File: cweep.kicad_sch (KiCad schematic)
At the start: 51 parts

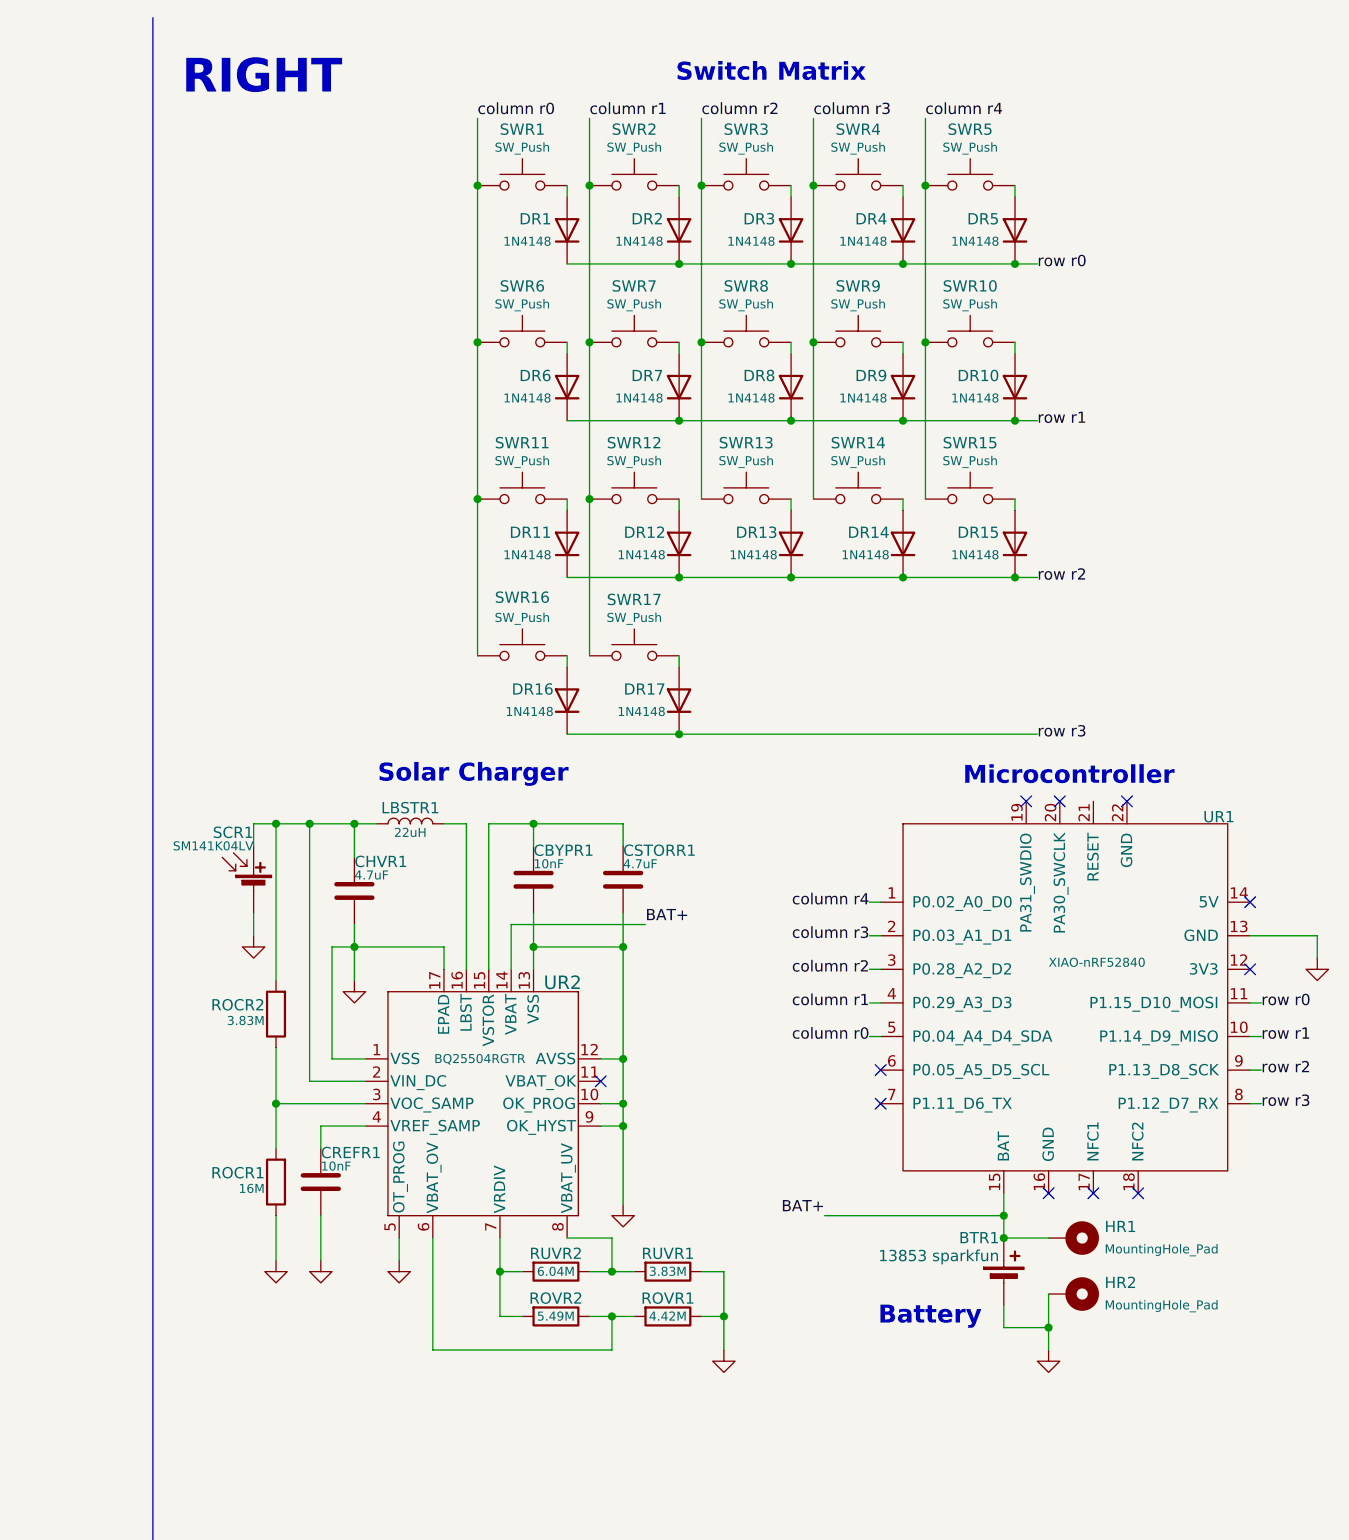
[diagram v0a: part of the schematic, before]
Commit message: feat: add reset button and power switch
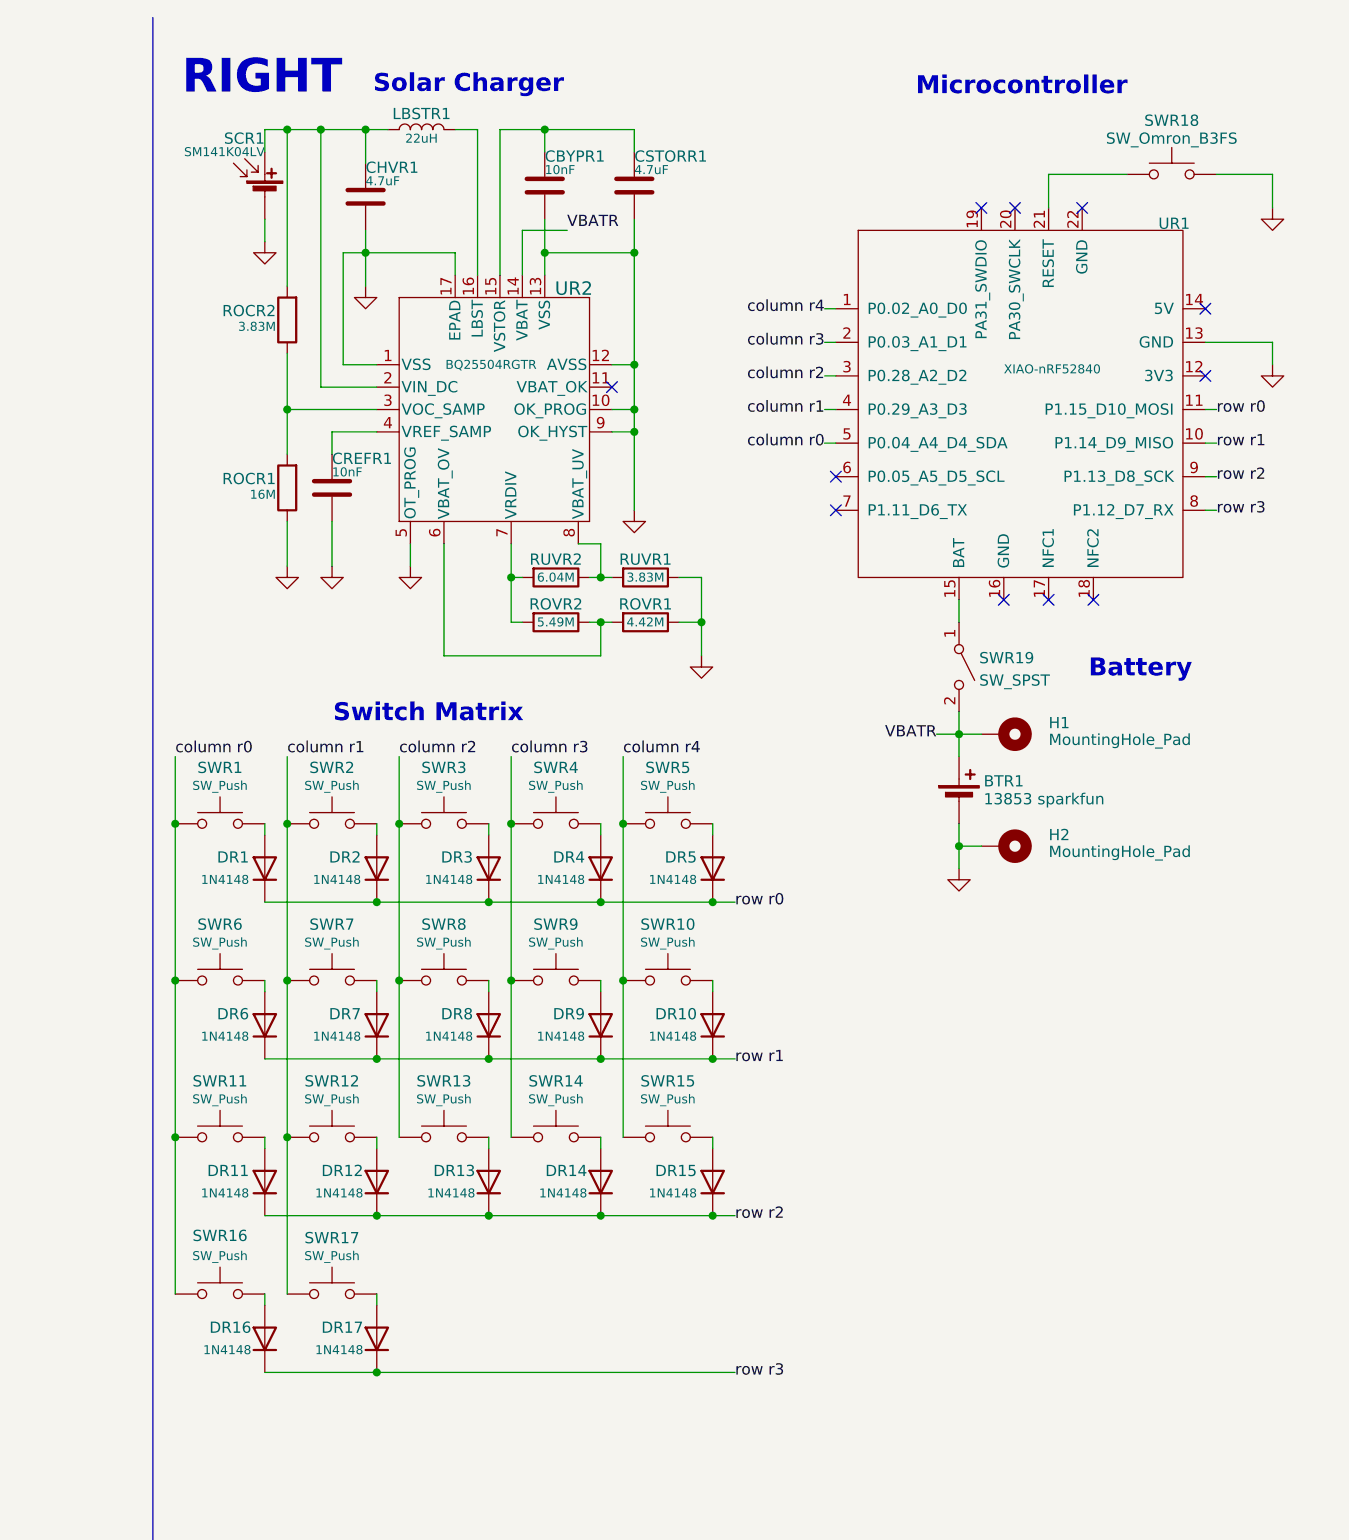
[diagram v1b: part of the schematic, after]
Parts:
- added SWR18: SW_Omron_B3FS, Button_Switch_THT:SW_TH_Tactile_Omron_B3F-10xx, symbol Switch:SW_Omron_B3FS
- added SWR19: SW_SPST, KAN-15:SW_KAN-15_PHT, symbol Switch:SW_SPST
- renumbered HR1 to H1, HR2 to H2
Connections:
- net GND: now also SWR18.2
- net at UR1.21 (RESET): now also SWR18.1
- net BAT+ renamed VBATR
- net VBATR: now also SWR19.2 (B); no longer UR1.15 (BAT)
- new net: SWR19.1 (A), UR1.15 (BAT)
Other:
- moved on the sheet: BTR1, CBYPR1, CHVR1, CREFR1, CSTORR1, DR1, DR10, DR11, DR12, DR13, DR14, DR15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

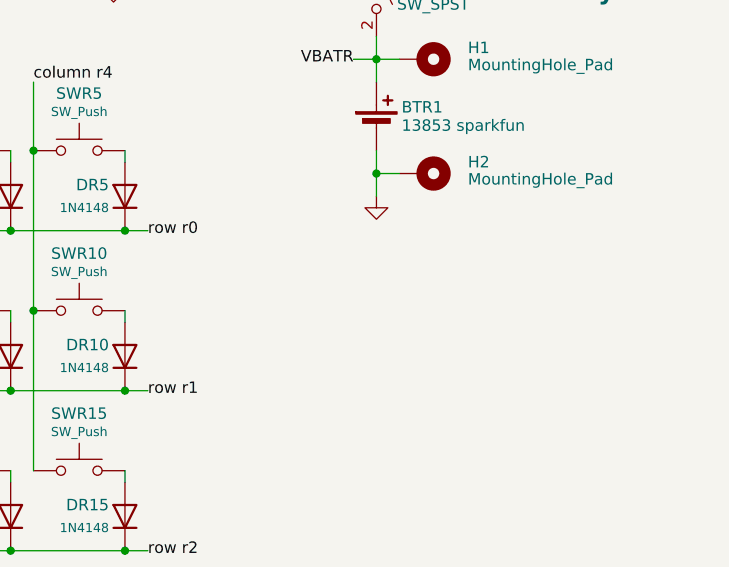
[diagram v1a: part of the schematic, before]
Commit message: fix: connect solar components to top pogo pin
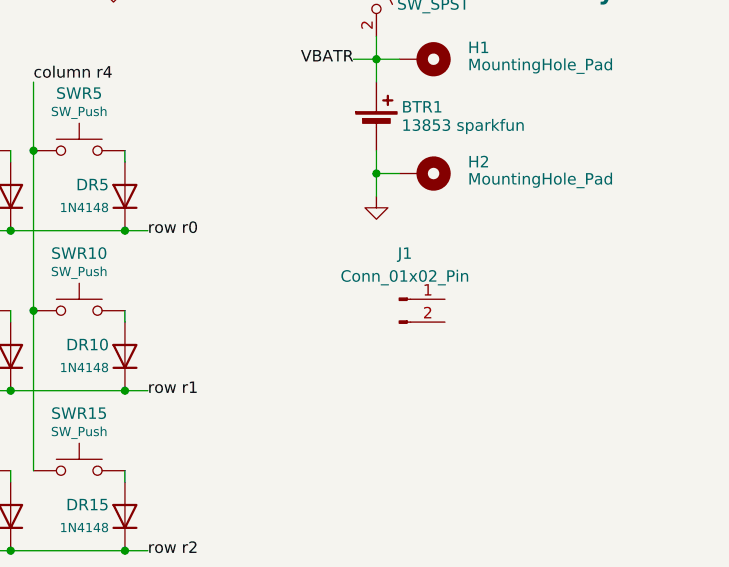
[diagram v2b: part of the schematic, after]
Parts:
- added J1: Conn_01x02_Pin, Connector_JST:JST_PH_S2B-PH-K_1x02_P2.00mm_Horizontal, symbol Connector:Conn_01x02_Pin
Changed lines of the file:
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@@
+	)
+	(symbol
+		(lib_id "Connector:Conn_01x02_Pin")
+		(at 242.57 118.11 0)
+		(unit 1)
+		(exclude_from_sim no)
+		(in_bom yes)
+		(on_board yes)
+		(dnp no)
+		(fields_autoplaced yes)
+		(property "Reference" "J1"
+			(at 243.205 113.03 0)
+			(effects
+				(font
+					(size 1.27 1.27)
+				)
+			)
+		)
+		(property "Value" "Conn_01x02_Pin"
+			(at 243.205 115.57 0)
+			(effects
+				(font
+					(size 1.27 1.27)
+				)
+			)
+		)
+		(property "Footprint" "Connector_JST:JST_PH_S2B-PH-K_1x02_P2.00mm_Horizontal"
+			(at 242.57 118.11 0)
+			(effects
+				(font
+					(size 1.27 1.27)
+				)
+				(hide yes)
+			)
+		)
+		(property "Datasheet" "~"
+			(at 242.57 118.11 0)
+			(effects
+				(font
+					(size 1.27 1.27)
+				)
+				(hide yes)
+			)
+		)
+		(property "Description" "Generic connector, single row, 01x02, script generated"
+			(at 242.57 118.11 0)
+			(effects
+				(font
+					(size 1.27 1.27)
+				)
+				(hide yes)
+			)
+		)
+		(pin "1"
+		)
+		(pin "2"
+		)
+		(instances
+			(project ""
+				(path "/639fa181-da29-4b09-bbdd-4ee6b511df9a"
+					(reference "J1")
+					(unit 1)
+				)
+			)
+		)
 	)
 	(symbol

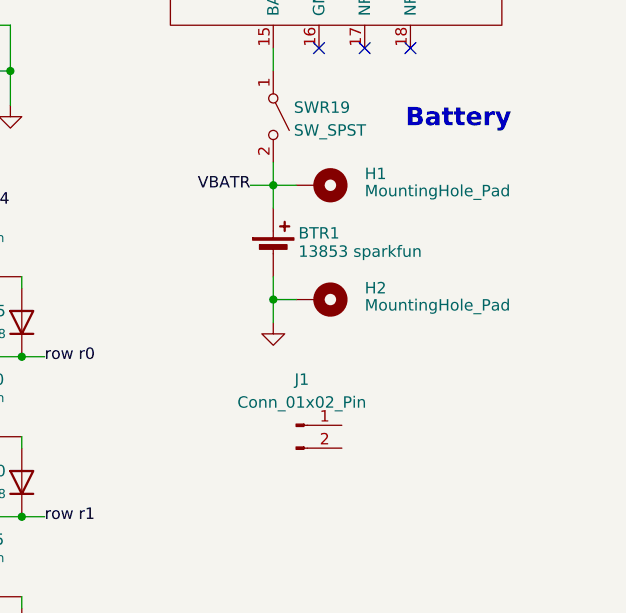
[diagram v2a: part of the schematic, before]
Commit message: feat: battery capacity 110mAh -> 350mAh
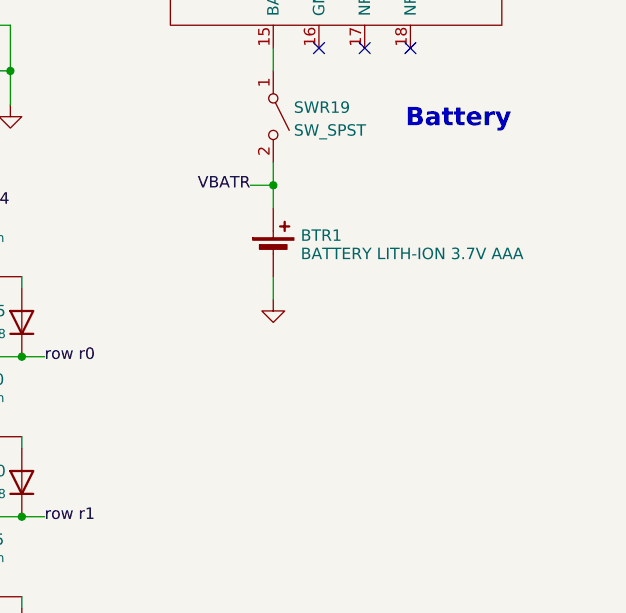
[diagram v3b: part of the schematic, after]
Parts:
- removed H1, H2: MountingHole_Pad, cweep:UL3302AWG#26, symbol Mechanical:MountingHole_Pad
- removed J1: Conn_01x02_Pin, Connector_JST:JST_PH_S2B-PH-K_1x02_P2.00mm_Horizontal, symbol Connector:Conn_01x02_Pin
- BTR1: value 13853 sparkfun -> BATTERY LITH-ION 3.7V AAA; footprint cweep:13853-sparkfun -> com_snapeda_Keystone:BatteryHolder_Keystone_230-1_1xAAA

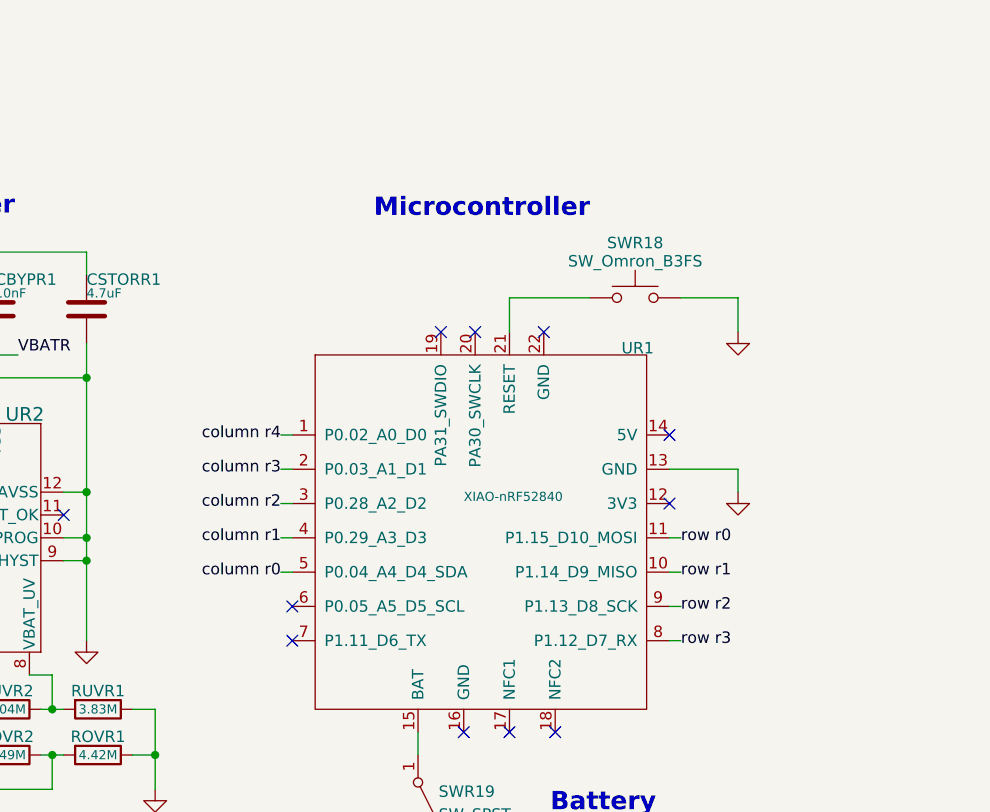
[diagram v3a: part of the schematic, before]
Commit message: fix: re-attach traces for gpio, power, and reset switches
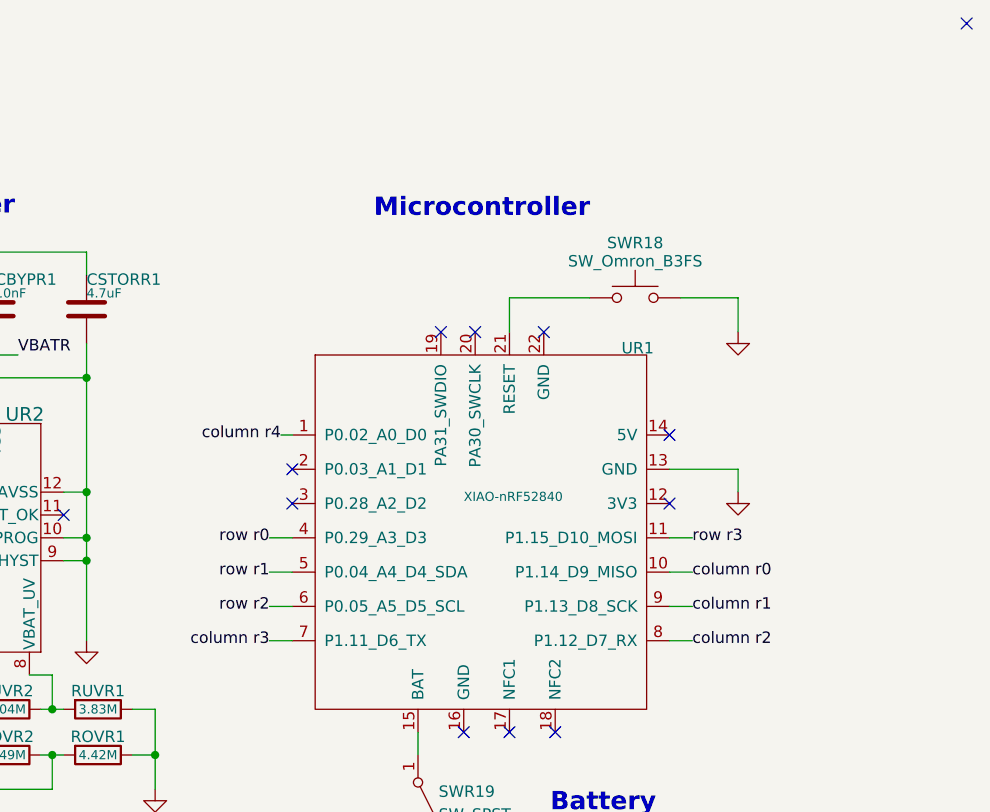
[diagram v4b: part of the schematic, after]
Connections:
- net column r0: now also UR1.10 (P1.14_D9_MISO); no longer UR1.5 (P0.04_A4_D4_SDA)
- net column r1: now also UR1.9 (P1.13_D8_SCK); no longer UR1.4 (P0.29_A3_D3)
- net column r2: now also UR1.8 (P1.12_D7_RX); no longer UR1.3 (P0.28_A2_D2)
- net column r3: now also UR1.7 (P1.11_D6_TX); no longer UR1.2 (P0.03_A1_D1)
- net row r0: now also UR1.4 (P0.29_A3_D3); no longer UR1.11 (P1.15_D10_MOSI)
- net row r1: now also UR1.5 (P0.04_A4_D4_SDA); no longer UR1.10 (P1.14_D9_MISO)
- net row r2: now also UR1.6 (P0.05_A5_D5_SCL); no longer UR1.9 (P1.13_D8_SCK)
- net row r3: now also UR1.11 (P1.15_D10_MOSI); no longer UR1.8 (P1.12_D7_RX)
- no-connect marks 11 -> 12
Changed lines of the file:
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@@
-	)
-	(no_connect
-		(at 226.06 62.23)
 	)
 	(no_connect
@@
 	)
 	(no_connect
+		(at 226.06 46.99)
+	)
+	(no_connect
 		(at 267.97 43.18)
-	)
-	(no_connect
-		(at 226.06 66.04)
 	)
 	(no_connect
@@
 	)
 	(no_connect
+		(at 300.99 -2.54)
+	)
+	(no_connect
 		(at 246.38 31.75)
 	)
-	(wire
-		(pts
-			(xy 267.97 62.23) (xy 269.24 62.23)
-		)
-		(stroke
-			(width 0)
-			(type default)
-		)
+	(no_connect
+		(at 226.06 50.8)
 	)
 	(wire
@@
 	(wire
 		(pts
+			(xy 223.52 66.04) (xy 226.06 66.04)
+		)
+		(stroke
+			(width 0)
+			(type default)
+		)
+	)
+	(wire
+		(pts
 			(xy 172.72 36.83) (xy 182.88 36.83)
 		)
@@
 	(wire
 		(pts
+			(xy 270.51 66.04) (xy 267.97 66.04)
+		)
+		(stroke
+			(width 0)
+			(type default)
+		)
+	)
+	(wire
+		(pts
 			(xy 163.83 72.39) (xy 163.83 67.31)
 		)
@@
 	(wire
 		(pts
-			(xy 224.79 50.8) (xy 226.06 50.8)
-		)
-		(stroke
-			(width 0)
-			(type default)
-		)
-	)
-	(wire
-		(pts
 			(xy 161.29 119.38) (xy 161.29 120.65)
 		)
@@
 	(wire
 		(pts
-			(xy 267.97 58.42) (xy 269.24 58.42)
-		)
-		(stroke
-			(width 0)
-			(type default)
-		)
-	)
-	(wire
-		(pts
-			(xy 224.79 54.61) (xy 226.06 54.61)
-		)
-		(stroke
-			(width 0)
-			(type default)
-		)
-	)
-	(wire
-		(pts
 			(xy 173.99 146.05) (xy 186.69 146.05)
 		)
@@
 		)
 	)
-	(wire
-		(pts
-			(xy 267.97 54.61) (xy 269.24 54.61)
-		)
-		(stroke
-			(width 0)
-			(type default)
-		)
-	)
 	(polyline
 		(pts
@@
 	(wire
 		(pts
-			(xy 224.79 58.42) (xy 226.06 58.42)
-		)
-		(stroke
-			(width 0)
-			(type default)
-		)
-	)
-	(wire
-		(pts
 			(xy 250.19 27.94) (xy 250.19 31.75)
 		)
@@
 	(wire
 		(pts
+			(xy 223.52 58.42) (xy 226.06 58.42)
+		)
+		(stroke
+			(width 0)
+			(type default)
+		)
+	)
+	(wire
+		(pts
 			(xy 170.18 49.53) (xy 173.99 49.53)
 		)
@@
 	(wire
 		(pts
+			(xy 270.51 62.23) (xy 267.97 62.23)
+		)
+		(stroke
+			(width 0)
+			(type default)
+		)
+	)
+	(wire
+		(pts
 			(xy 172.72 22.86) (xy 172.72 26.67)
 		)
@@
 	(wire
 		(pts
+			(xy 270.51 58.42) (xy 267.97 58.42)
+		)
+		(stroke
+			(width 0)
+			(type default)
+		)
+	)
+	(wire
+		(pts
 			(xy 161.29 25.4) (xy 161.29 22.86)
 		)
@@
 	(wire
 		(pts
+			(xy 223.52 54.61) (xy 226.06 54.61)
+		)
+		(stroke
+			(width 0)
+			(type default)
+		)
+	)
+	(wire
+		(pts
 			(xy 161.29 137.16) (xy 161.29 138.43)
 		)
@@
 	(wire
 		(pts
-			(xy 224.79 46.99) (xy 226.06 46.99)
-		)
-		(stroke
-			(width 0)
-			(type default)
-		)
-	)
-	(wire
-		(pts
 			(xy 173.99 57.15) (xy 168.91 57.15)
 		)
@@
 	(wire
 		(pts
+			(xy 223.52 62.23) (xy 226.06 62.23)
+		)
+		(stroke
+			(width 0)
+			(type default)
+		)
+	)
+	(wire
+		(pts
 			(xy 237.49 91.44) (xy 240.03 91.44)
 		)
@@
 	(wire
 		(pts
+			(xy 270.51 54.61) (xy 267.97 54.61)
+		)
+		(stroke
+			(width 0)
+			(type default)
+		)
+	)
+	(wire
+		(pts
 			(xy 203.2 33.02) (xy 203.2 36.83)
 		)
@@
 		(pts
 			(xy 193.04 33.02) (xy 193.04 36.83)
-		)
-		(stroke
-			(width 0)
-			(type default)
-		)
-	)
-	(wire
-		(pts
-			(xy 267.97 66.04) (xy 269.24 66.04)
 		)
 		(stroke
@@
 	)
 	(label "row r3"
-		(at 269.24 66.04 0)
+		(at 270.51 54.61 0)
 		(effects
 			(font
@@
 	)
 	(label "column r3"
-		(at 224.79 46.99 180)
+		(at 223.52 66.04 180)
 		(effects
 			(font
@@
 	)
 	(label "row r0"
-		(at 269.24 54.61 0)
-		(effects
-			(font
-				(size 1.27 1.27)
-			)
-			(justify left)
+		(at 223.52 54.61 180)
+		(effects
+			(font
+				(size 1.27 1.27)
+			)
+			(justify right)
 		)
 	)
@@
 	)
 	(label "column r0"
-		(at 224.79 58.42 180)
-		(effects
-			(font
-				(size 1.27 1.27)
-			)
-			(justify right)
+		(at 270.51 58.42 0)
+		(effects
+			(font
+				(size 1.27 1.27)
+			)
+			(justify left)
 		)
 	)
@@
 	)
 	(label "row r1"
-		(at 269.24 58.42 0)
-		(effects
-			(font
-				(size 1.27 1.27)
-			)
-			(justify left)
+		(at 223.52 58.42 180)
+		(effects
+			(font
+				(size 1.27 1.27)
+			)
+			(justify right)
 		)
 	)
@@
 	)
 	(label "row r2"
-		(at 269.24 62.23 0)
+		(at 223.52 62.23 180)
+		(effects
+			(font
+				(size 1.27 1.27)
+			)
+			(justify right)
+		)
+	)
+	(label "column r1"
+		(at 270.51 62.23 0)
 		(effects
 			(font
@@
 		)
 	)
-	(label "column r1"
-		(at 224.79 54.61 180)
-		(effects
-			(font
-				(size 1.27 1.27)
-			)
-			(justify right)
-		)
-	)
 	(label "column r2"
-		(at 224.79 50.8 180)
-		(effects
-			(font
-				(size 1.27 1.27)
-			)
-			(justify right)
-		)
-	)
+		(at 270.51 66.04 0)
+		(effects
+			(font
+				(size 1.27 1.27)
+			)
+			(justify left)
+		)
+	)
